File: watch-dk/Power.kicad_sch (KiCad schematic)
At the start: 26 parts, among them IC101 nPM1300-QEXX, X101 Battery, X102 Battery, X103 Power

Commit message: Task: Issue #124
Signed-off-by: Daniel Kampert <DanielKampert@kampis-elektroecke.de>
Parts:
- TP103: value 1V8 -> +1V8
- TP104: value 3V0 -> +3V0
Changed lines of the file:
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@@
 			)
 		)
-		(property "Value" "3V0"
+		(property "Value" "+3V0"
 			(at 203.2 102.743 0)
 			(effects
@@
 		)
 		(property "CONFIG" ""
+			(at 200.66 104.14 0)
+			(effects
+				(font
+					(size 1.27 1.27)
+				)
+				(hide yes)
+			)
+		)
+		(property "manf" ""
+			(at 200.66 104.14 0)
+			(effects
+				(font
+					(size 1.27 1.27)
+				)
+				(hide yes)
+			)
+		)
+		(property "manf#" ""
+			(at 200.66 104.14 0)
+			(effects
+				(font
+					(size 1.27 1.27)
+				)
+				(hide yes)
+			)
+		)
+		(property "mouser#" ""
 			(at 200.66 104.14 0)
 			(effects
@@
 			)
 		)
-		(property "Value" "1V8"
+		(property "Value" "+1V8"
 			(at 203.2 84.963 0)
 			(effects
@@
 			(at 200.66 86.36 0)
 			(effects
+				(font
+					(size 1.27 1.27)
+				)
+				(hide yes)
+			)
+		)
+		(property "manf" ""
+			(at 200.66 86.36 0)
+			(effects
+				(font
+					(size 1.27 1.27)
+				)
+				(hide yes)
+			)
+		)
+		(property "manf#" ""
+			(at 200.66 86.36 0)
+			(effects
+				(font
+					(size 1.27 1.27)
+				)
+				(hide yes)
+			)
+		)
+		(property "mouser#" ""
+			(at 200.66 86.36 0)
+			(effects

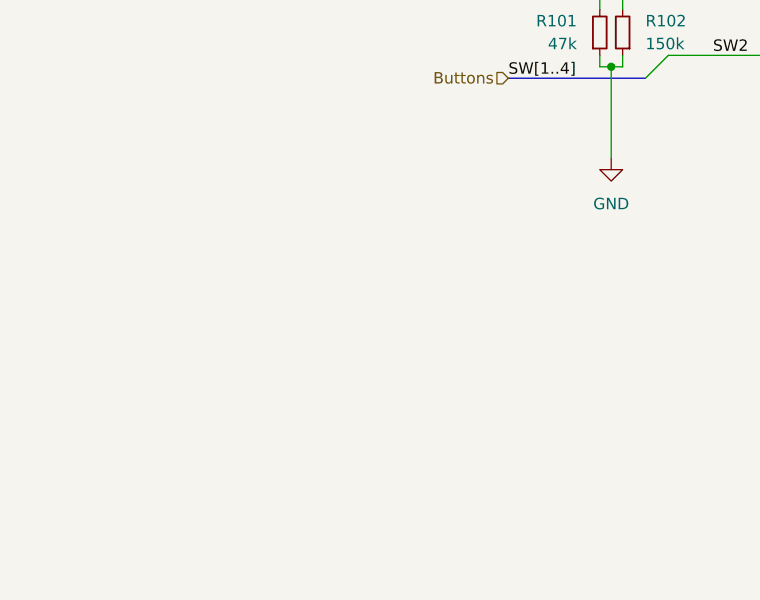
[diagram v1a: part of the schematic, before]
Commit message: Bug: Issue #127
Signed-off-by: Daniel Kampert <DanielKampert@kampis-elektroecke.de>
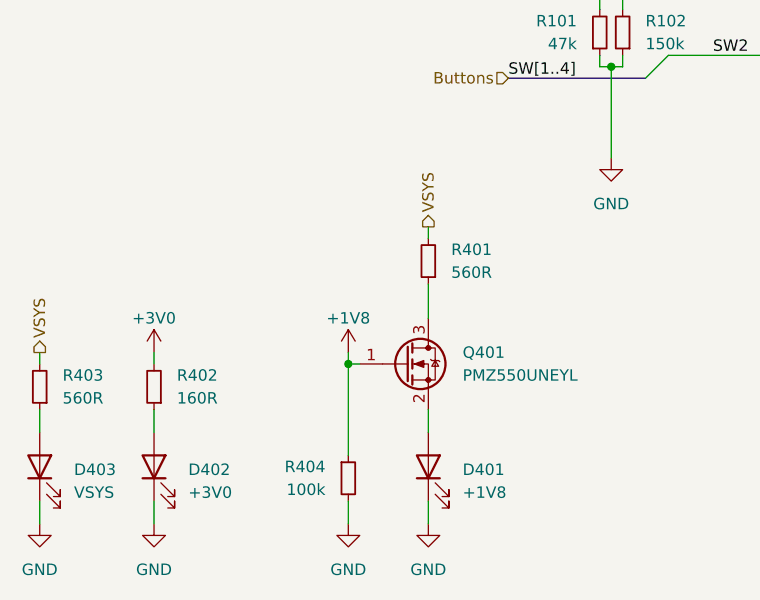
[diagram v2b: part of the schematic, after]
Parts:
- added D401: +1V8, LED_SMD:LED_0402_1005Metric, symbol Device:LED
- added D402: +3V0, LED_SMD:LED_0402_1005Metric, symbol Device:LED
- added D403: VSYS, LED_SMD:LED_0402_1005Metric, symbol Device:LED
- added Q401: PMZ550UNEYL, Package_SOT_SMD:SOT-883, symbol Nexperia:PMZ550UNEYL
- added R401, R403: 560R, Resistor_SMD:R_0402_1005Metric, symbol Device:R_Small
- added R402: 160R, Resistor_SMD:R_0402_1005Metric, symbol Device:R_Small
- added R404: 100k, Resistor_SMD:R_0402_1005Metric, symbol Device:R_Small
- R102: mouser# RC0402FR-07150KL -> 603-RC0402FR-07150KL
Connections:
- net +1V8: now also Q401.1 (G), R404.1
- net +3V0: now also R402.2
- net GND: now also D401.1 (K), D402.1 (K), D403.1 (K), R404.2
- net VSYS: now also R401.2, R403.2
- new net: D402.2 (A), R402.1
- new net: D403.2 (A), R403.1
- new net: D401.2 (A), Q401.2 (S)
- new net: Q401.3 (D), R401.1

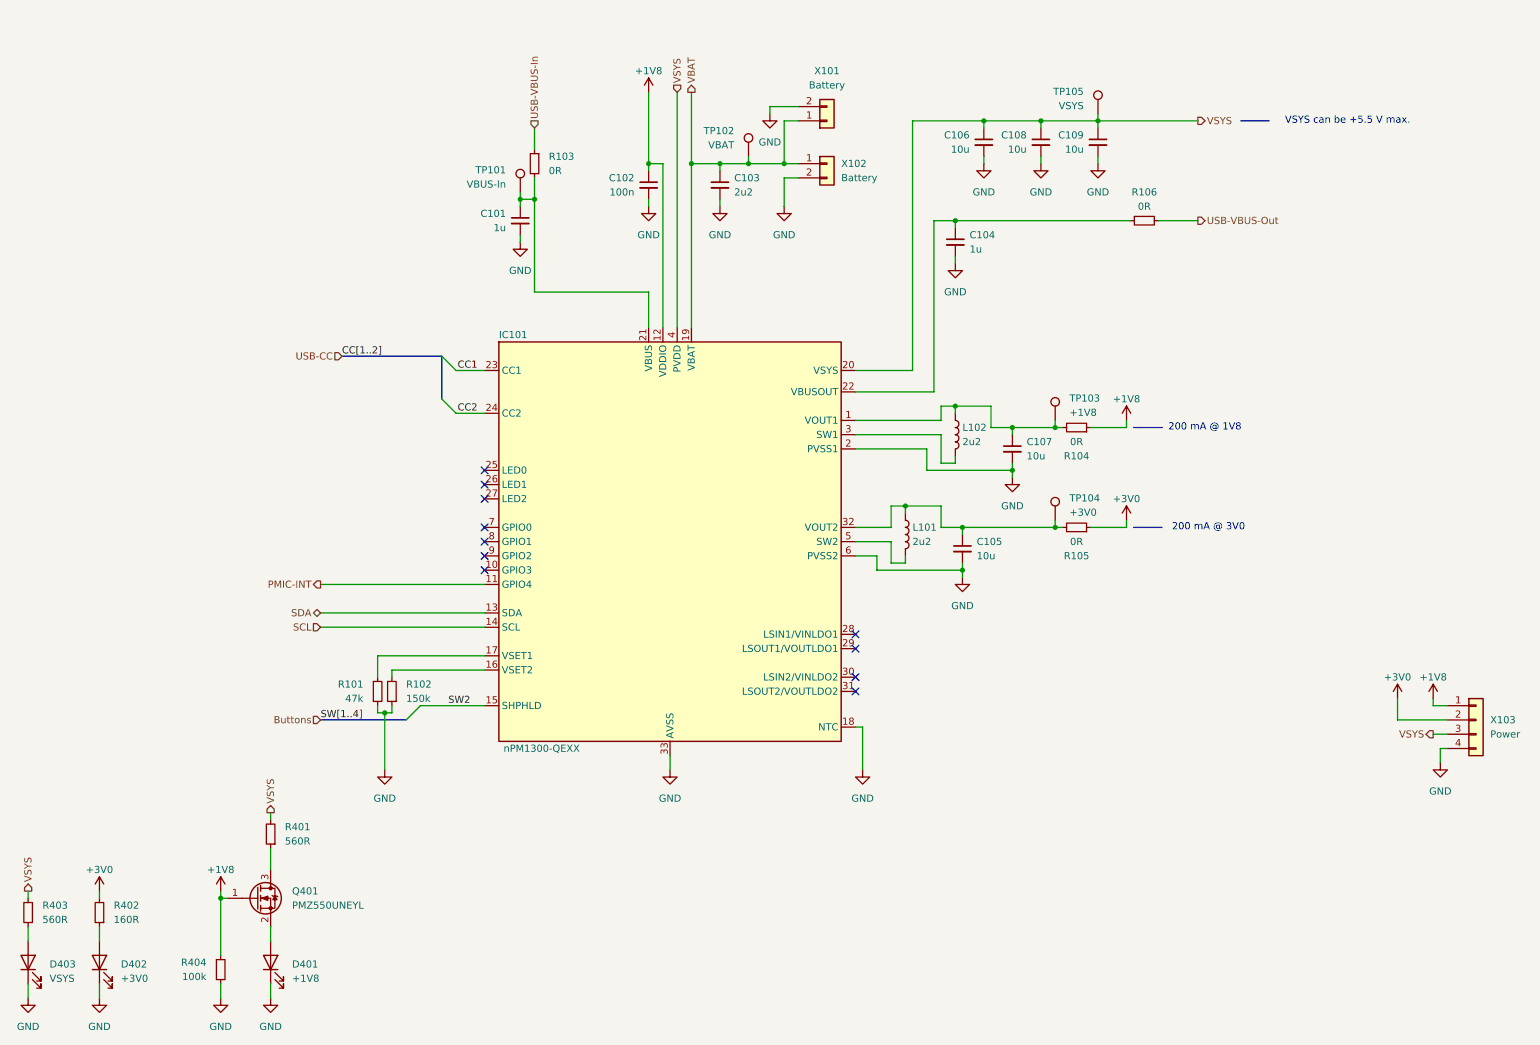
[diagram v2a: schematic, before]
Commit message: Task: Issue #130
Signed-off-by: Daniel Kampert <DanielKampert@kampis-elektroecke.de>
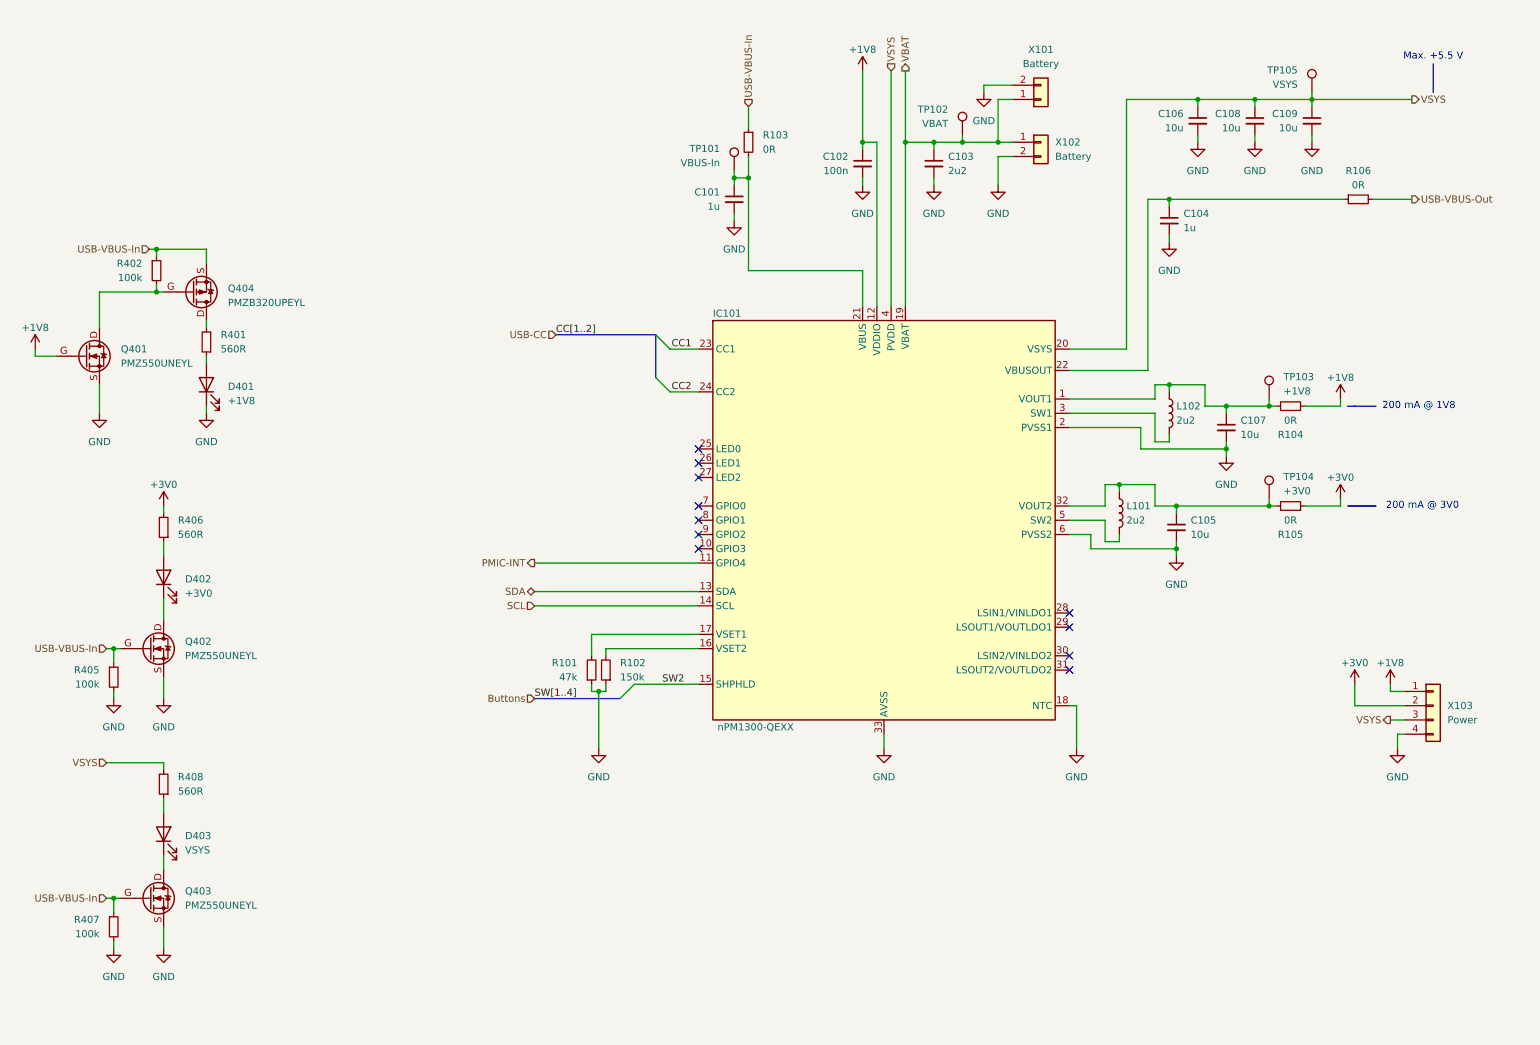
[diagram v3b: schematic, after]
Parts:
- removed R403: 560R, Resistor_SMD:R_0402_1005Metric, symbol Device:R_Small
- removed R404: 100k, Resistor_SMD:R_0402_1005Metric, symbol Device:R_Small
- added Q402, Q403: PMZ550UNEYL, Package_DFN_Kampi:DFN-1006-3, symbol Nexperia:PMZ550UNE
- added Q404: PMZB320UPEYL, Package_DFN_Kampi:DFN-1006-3, symbol Nexperia:PMZB320UPE
- added R405, R407: 100k, Resistor_SMD:R_0402_1005Metric, symbol Device:R_Small
- added R406, R408: 560R, Resistor_SMD:R_0402_1005Metric, symbol Device:R_Small
- Q401: footprint Package_SOT_SMD:SOT-883 -> Package_DFN_Kampi:DFN-1006-3; symbol Nexperia:PMZ550UNEYL -> Nexperia:PMZ550UNE
- R402: value 160R -> 100k; manf# RC0402FR-07160RL -> RC0404FR-07100KL; mouser# 603-RC0402FR-07160RL -> 603-RC0404FR-07100KL
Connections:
- net +1V8: now also Q401.G; no longer Q401.1 (G)
- net +3V0: now also R406.2; no longer R402.2
- net GND: now also Q401.S, Q402.S, Q403.S, R405.2, R407.2; no longer D402.1 (K), D403.1 (K)
- net USB-VBUS-In: now also R402.1, Q402.G, Q403.G, Q404.S, R405.1, R407.1
- net VSYS: now also R408.2; no longer R401.2
- net at D402.2 (A): now also R406.1; no longer R402.1
- net at D403.2 (A): now also R408.1
- net at D401.2 (A): now also R401.1; no longer Q401.2 (S)
- new net: D402.1 (K), Q402.D
- new net: D403.1 (K), Q403.D
- new net: Q404.D, R401.2
- new net: Q401.D, Q404.G, R402.2
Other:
- note added: "Max. +5.5 V"
- note removed: "VSYS can be +5.5 V max."
- moved on the sheet: C101, C102, C103, C104, C105, C106, C107, C108, C109, D401, D402, D403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

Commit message: Feature: Issue #131
- Fix wrong page numbers
- Update reference designators to match the page numbers

Signed-off-by: Daniel Kampert <DanielKampert@kampis-elektroecke.de>
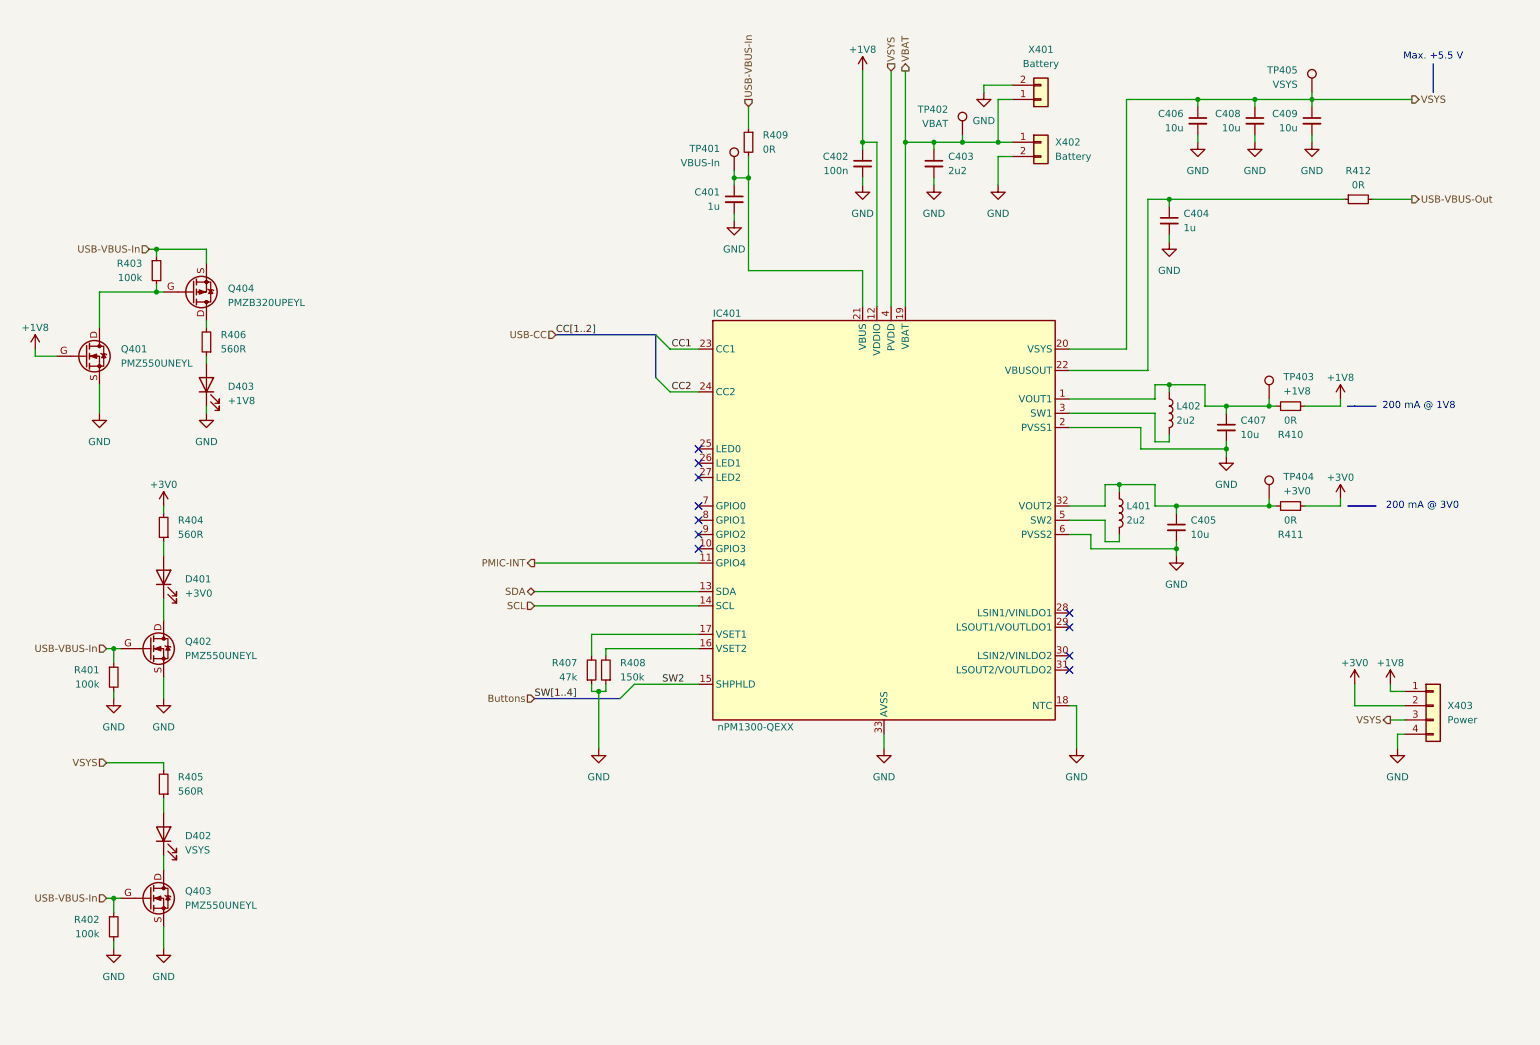
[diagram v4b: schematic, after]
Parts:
- renumbered C101 to C401, C102 to C402, C103 to C403, C104 to C404, C105 to C405, C106 to C406, C107 to C407, C108 to C408, C109 to C409, D402 to D401, D403 to D402, D401 to D403, IC101 to IC401, L101 to L401, L102 to L402, R405 to R401, R407 to R402, R402 to R403, R406 to R404, R408 to R405, R401 to R406, R101 to R407, R102 to R408, R103 to R409, R104 to R410, R105 to R411, R106 to R412, TP101 to TP401, TP102 to TP402, TP103 to TP403, TP104 to TP404, TP105 to TP405, X101 to X401, X102 to X402, X103 to X403

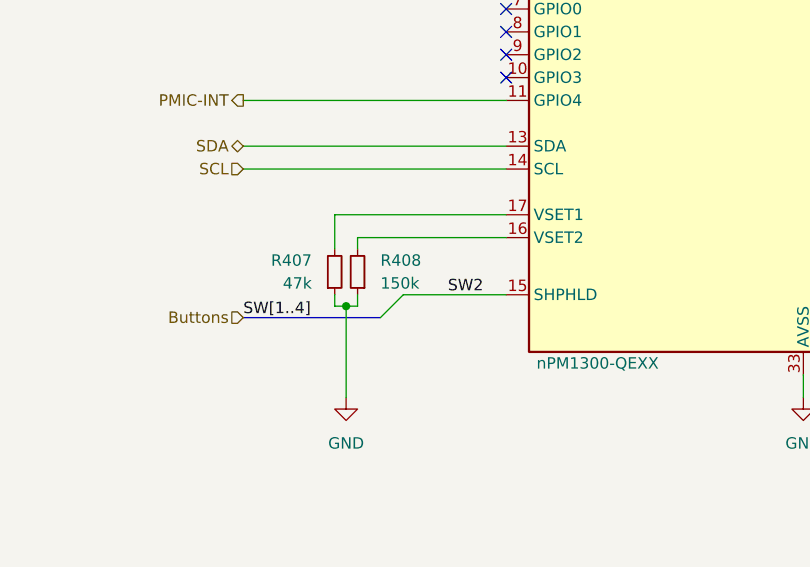
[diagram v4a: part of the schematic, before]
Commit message: Feature: Issue #133
Signed-off-by: Daniel Kampert <DanielKampert@kampis-elektroecke.de>
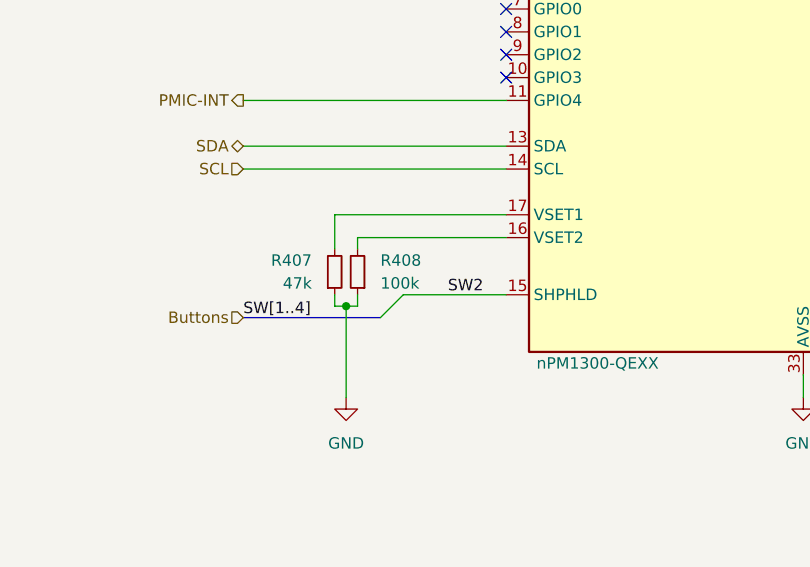
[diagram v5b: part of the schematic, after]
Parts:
- R408: value 150k -> 100k; manf# RC0402FR-07150KL -> RC0404FR-07100KL; mouser# 603-RC0402FR-07150KL -> 603-RC0404FR-07100KL
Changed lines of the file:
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@@
 			)
 		)
-		(property "Value" "150k"
+		(property "Value" "100k"
 			(at 123.19 132.08 0)
 			(effects
@@
 			)
 		)
-		(property "manf#" "RC0402FR-07150KL"
+		(property "manf#" "RC0404FR-07100KL"
 			(at 120.65 130.81 0)
 			(effects
@@
 			)
 		)
-		(property "mouser#" "603-RC0402FR-07150KL"
+		(property "mouser#" "603-RC0404FR-07100KL"
 			(at 120.65 130.81 0)
 			(effects
